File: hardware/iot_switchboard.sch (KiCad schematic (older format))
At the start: 14 parts, among them IC1 ATTINY44A-SS, P1 CONN_01X05, P2 AVR_ISP

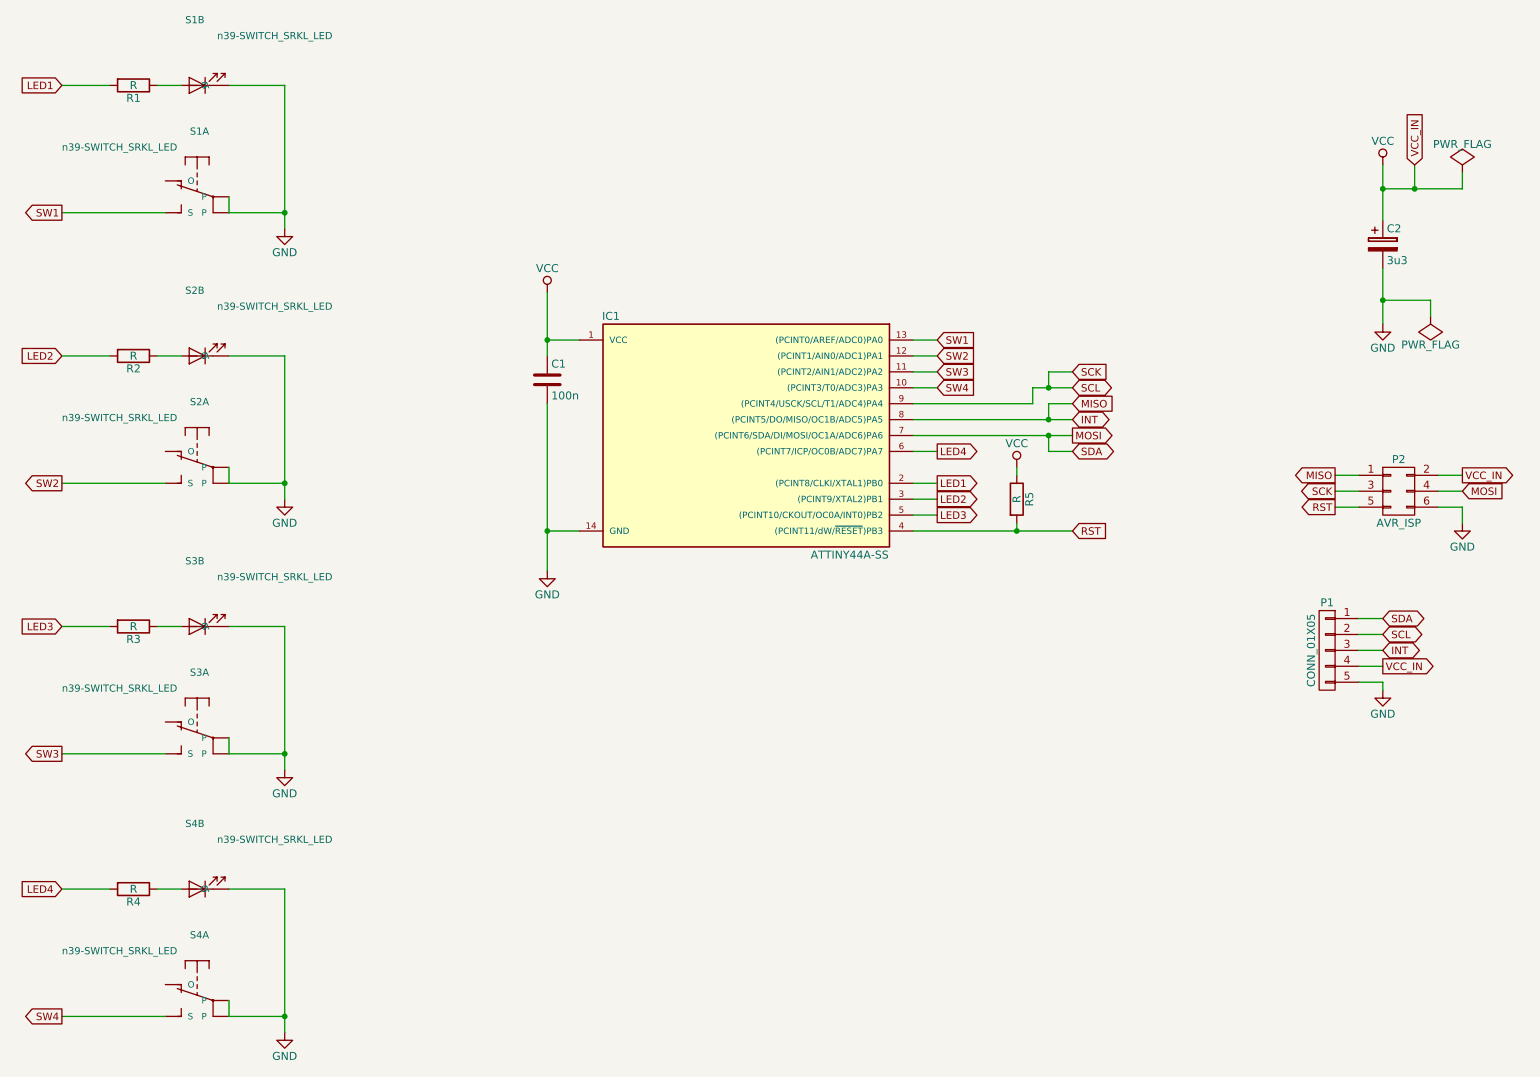
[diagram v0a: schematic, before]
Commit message: layout and attiny in QFN20
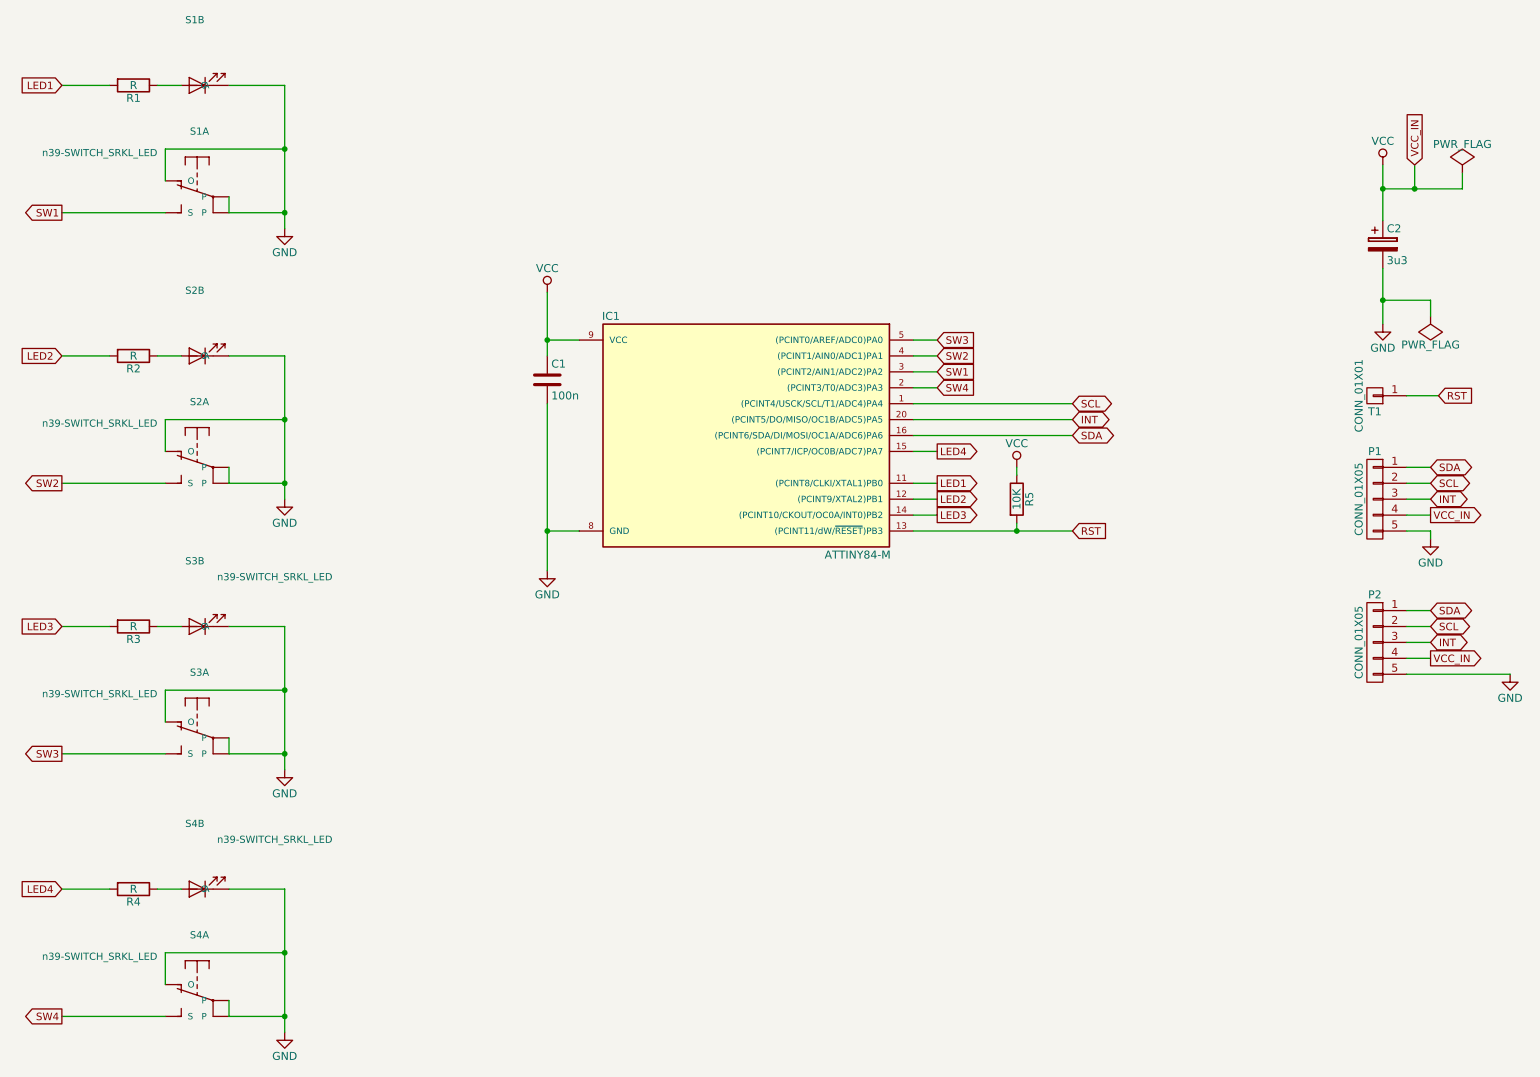
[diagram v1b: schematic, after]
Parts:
- removed IC1: ATTINY44A-SS, Housings_SOIC:SOIC-14_3.9x8.7mm_Pitch1.27mm, symbol ATTINY44A-SS
- removed P2: AVR_ISP, Socket_Strips:Socket_Strip_Angled_2x03, symbol CONN_02X03
- added IC1: ATTINY84-M, Housings_DFN_QFN:QFN-20-1EP_4x4mm_Pitch0.5mm, symbol ATTINY84-M
- added P2: CONN_01X05, Socket_Strips:Socket_Strip_Straight_1x05, symbol CONN_01X05
- added T1: CONN_01X01, Measurement_Points:Measurement_Point_Round-TH_Small, symbol CONN_01X01
- R5: value R -> 10K
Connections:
- net GND: now also S1.4 (O), S2.4 (O), S3.4 (O), S4.4 (O), IC1.8 (GND), P2.5 (P5)
- net INT: now also IC1.20 ((PCINT5/DO/MISO/OC1B/ADC5)PA5), P2.3 (P3)
- net LED1: now also IC1.11 ((PCINT8/CLKI/XTAL1)PB0)
- net LED2: now also IC1.12 ((PCINT9/XTAL2)PB1)
- net LED3: now also IC1.14 ((PCINT10/CKOUT/OC0A/INT0)PB2)
- net LED4: now also IC1.15 ((PCINT7/ICP/OC0B/ADC7)PA7)
- net RST: now also IC1.13 ((PCINT11/dW/~RESET~)PB3), T1.1 (P1)
- net SW1: now also IC1.3 ((PCINT2/AIN1/ADC2)PA2)
- net SW2: now also IC1.4 ((PCINT1/AIN0/ADC1)PA1)
- net SW3: now also IC1.5 ((PCINT0/AREF/ADC0)PA0)
- net SW4: now also IC1.2 ((PCINT3/T0/ADC3)PA3)
- net VCC: now also IC1.9 (VCC), P2.4 (P4)
- net MOSI renamed SDA
- net SDA: now also IC1.16 ((PCINT6/SDA/DI/MOSI/OC1A/ADC6)PA6), P2.1 (P1)
- net SCK renamed SCL
- net SCL: now also IC1.1 ((PCINT4/USCK/SCL/T1/ADC4)PA4), P2.2 (P2)
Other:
- moved on the sheet: P1

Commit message: Replace load capacitor by 0603 type
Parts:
- C2: footprint Capacitors_Tantalum_SMD:Tantalum_Case-B_EIA-3528-21_Hand -> Capacitors_SMD:C_0603_HandSoldering
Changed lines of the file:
@@
 F 0 "C2" H 9375 2350 50  0000 L CNN
 F 1 "3u3" H 9375 2150 50  0000 L CNN
-F 2 "Capacitors_Tantalum_SMD:Tantalum_Case-B_EIA-3528-21_Hand" H 9388 2100 50  0001 C CNN
+F 2 "Capacitors_SMD:C_0603_HandSoldering" H 9388 2100 50  0001 C CNN
 F 3 "" H 9350 2250 50  0000 C CNN
 F 4 "SMD TAN.3,3/16" H 9350 2250 60  0001 C CNN "Reichelt"
